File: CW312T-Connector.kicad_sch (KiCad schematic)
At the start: 3 parts, among them P1 PCIEx4 EDGE CONNECTOR

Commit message: updated design - still needs vcc routing
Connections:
- net CLKIN renamed CLKO_FROM_FPGA
- net CLKOUT renamed CLKI_TO_FPGA
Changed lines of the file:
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@@
 		)
 	)
-	(hierarchical_label "CLKIN"
+	(hierarchical_label "CLKO_FROM_FPGA"
 		(shape input)
 		(at 93.98 124.46 180)
@@
 		)
 	)
-	(hierarchical_label "CLKOUT"
+	(hierarchical_label "CLKI_TO_FPGA"
 		(shape input)
 		(at 199.39 119.38 0)

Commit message: updated schematic and pcb, fixed silkscreen - Ready for review
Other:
- moved on the sheet: R12, R13

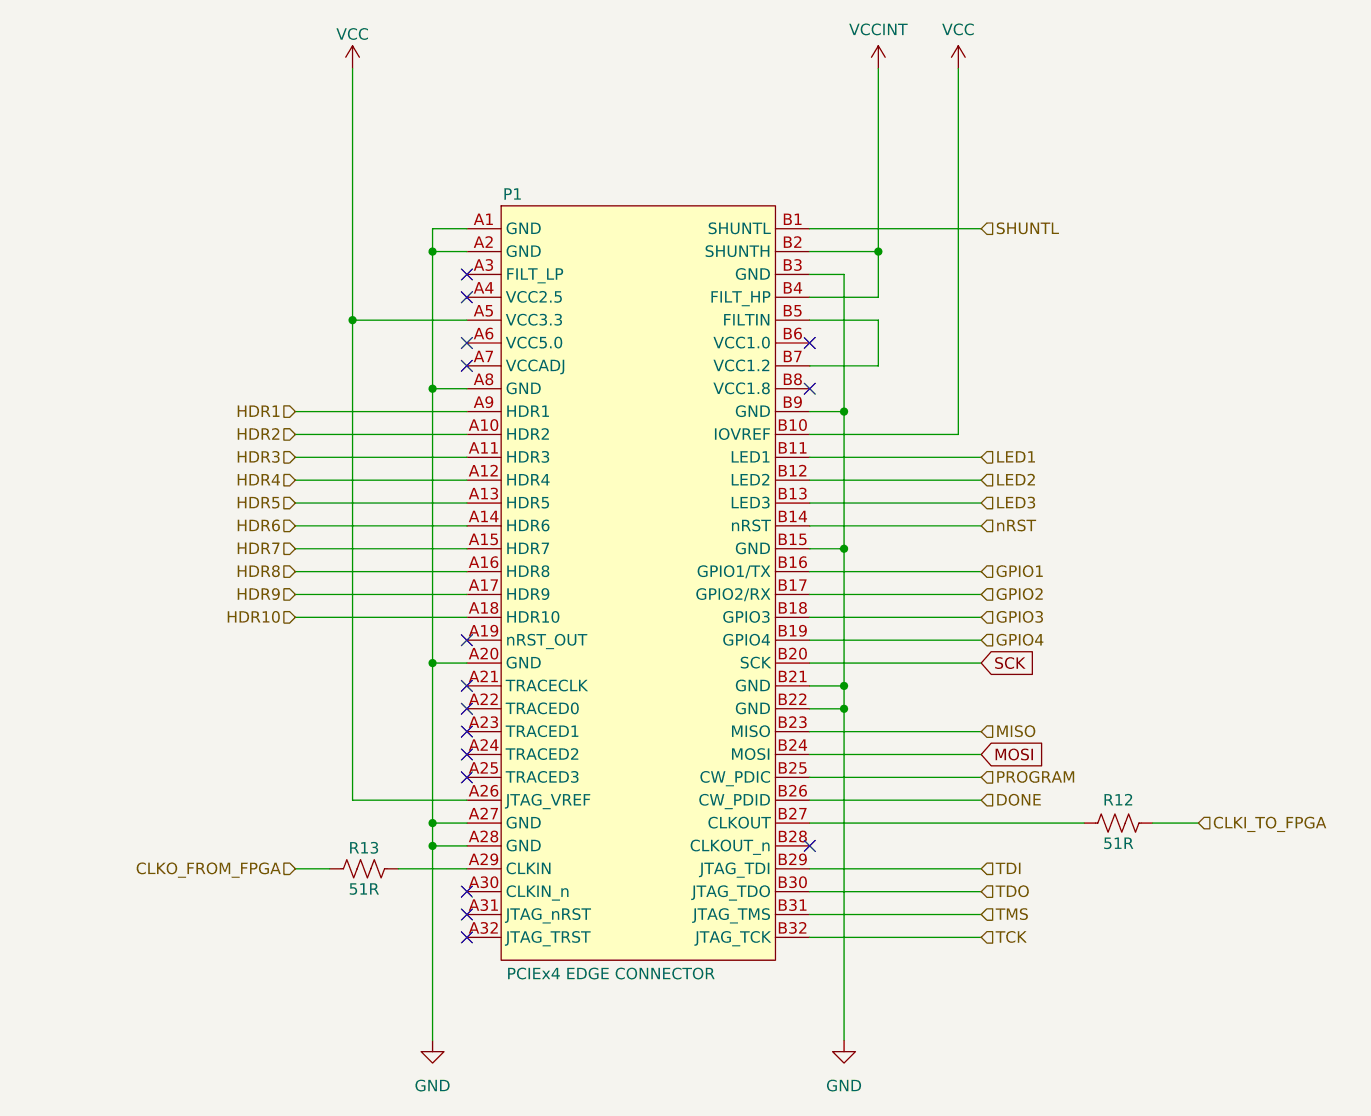
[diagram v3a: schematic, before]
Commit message: updated schematic and pcb after library re-organization
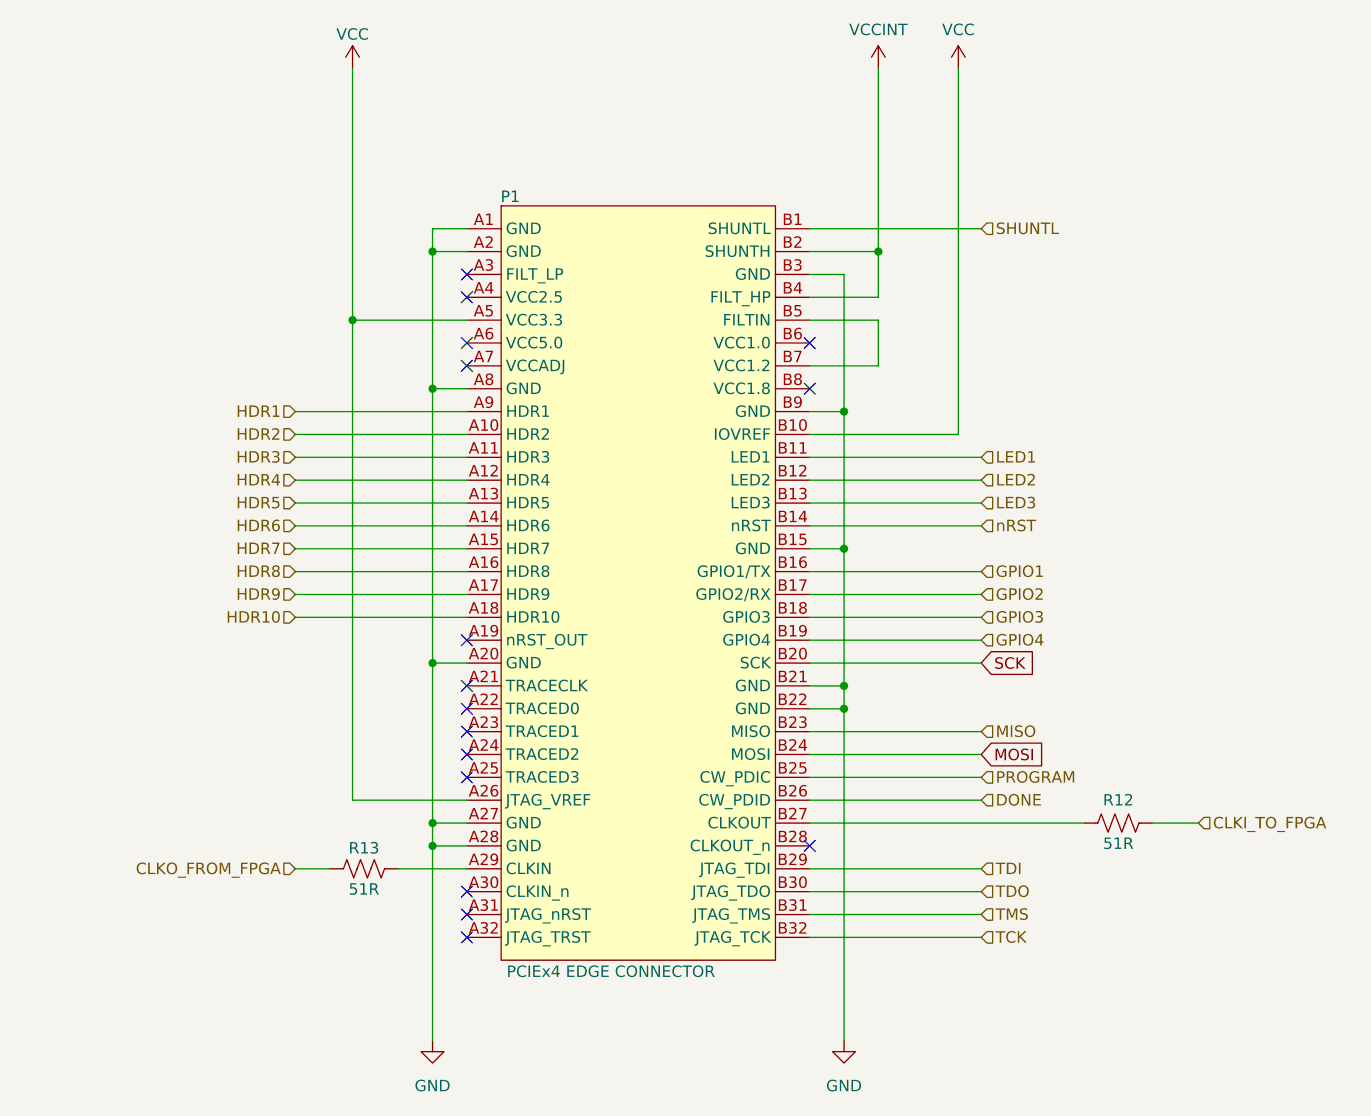
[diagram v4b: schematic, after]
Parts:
- removed P1: PCIEx4 EDGE CONNECTOR, tutorial_2_library:CW312_Template, symbol tutorial_2_library:CW312T-Template
- added P1: PCIEx4 EDGE CONNECTOR, tutorial_2_library:CW312_Template, symbol Connectors:CW312T-Template
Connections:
- net DONE: now also P1.B26 (CW_PDID)
- net GND: now also P1.A1 (GND), P1.A2 (GND), P1.A20 (GND), P1.A27 (GND), P1.A28 (GND), P1.A8 (GND), P1.B15 (GND), P1.B21 (GND), P1.B22 (GND), P1.B3 (GND), P1.B9 (GND)
- net GPIO1: now also P1.B16 (GPIO1/TX)
- net GPIO2: now also P1.B17 (GPIO2/RX)
- net GPIO3: now also P1.B18 (GPIO3)
- net GPIO4: now also P1.B19 (GPIO4)
- net HDR1: now also P1.A9 (HDR1)
- net HDR10: now also P1.A18 (HDR10)
- net HDR2: now also P1.A10 (HDR2)
- net HDR3: now also P1.A11 (HDR3)
- net HDR4: now also P1.A12 (HDR4)
- net HDR5: now also P1.A13 (HDR5)
- net HDR6: now also P1.A14 (HDR6)
- net HDR7: now also P1.A15 (HDR7)
- net HDR8: now also P1.A16 (HDR8)
- net HDR9: now also P1.A17 (HDR9)
- net LED1: now also P1.B11 (LED1)
- net LED2: now also P1.B12 (LED2)
- net LED3: now also P1.B13 (LED3)
- net MISO: now also P1.B23 (MISO)
- net MOSI: now also P1.B24 (MOSI)
- net PROGRAM: now also P1.B25 (CW_PDIC)
- net SCK: now also P1.B20 (SCK)
- net SHUNTL: now also P1.B1 (SHUNTL)
- net TCK: now also P1.B32 (JTAG_TCK)
- net TDI: now also P1.B29 (JTAG_TDI)
- net TDO: now also P1.B30 (JTAG_TDO)
- net TMS: now also P1.B31 (JTAG_TMS)
- net VCC: now also P1.A26 (JTAG_VREF), P1.A5 (VCC3.3), P1.B10 (IOVREF)
- net VCCINT: now also P1.B2 (SHUNTH), P1.B4 (FILT_HP)
- net nRST: now also P1.B14 (nRST)
- net at R13.2: now also P1.A29 (CLKIN)
- net at R12.1: now also P1.B27 (CLKOUT)
- new net: P1.B5 (FILTIN), P1.B7 (VCC1.2)
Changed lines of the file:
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@@
-	)
-	(symbol
-		(lib_id "tutorial_2_library:CW312T-Template")
-		(at 142.24 53.34 0)
-		(unit 1)
-		(exclude_from_sim no)
-		(in_bom no)
-		(on_board yes)
-		(dnp no)
-		(property "Reference" "P1"
-			(at 128.27 49.53 0)
-			(effects
-				(font
-					(size 1.27 1.27)
-				)
-			)
-		)
-		(property "Value" "PCIEx4 EDGE CONNECTOR"
-			(at 139.192 136.144 0)
-			(effects
-				(font
-					(size 1.27 1.27)
-				)
-			)
-		)
-		(property "Footprint" "tutorial_2_library:CW312_Template"
-			(at 138.43 146.05 0)
-			(effects
-				(font
-					(size 1.27 1.27)
-				)
-				(hide yes)
-			)
-		)
-		(property "Datasheet" ""
-			(at 139.7 52.07 0)
-			(effects
-				(font
-					(size 1.27 1.27)
-				)
-				(hide yes)
-			)
-		)
-		(property "Description" "BOARD AND EDGE CONNECTOR TEMPLATE FOR CW312 TARGETS"
-			(at 151.13 142.24 0)
-			(effects
-				(font
-					(size 1.27 1.27)
-				)
-				(hide yes)
-			)
-		)
-		(pin "B27"
-		)
-		(pin "B28"
-		)
-		(pin "B32"
-		)
-		(pin "B6"
-		)
-		(pin "B9"
-		)
-		(pin "B7"
-		)
-		(pin "B30"
-		)
-		(pin "B31"
-		)
-		(pin "B26"
-		)
-		(pin "B4"
-		)
-		(pin "B3"
-		)
-		(pin "B5"
-		)
-		(pin "B8"
-		)
-		(pin "B29"
-		)
-		(pin "B18"
-		)
-		(pin "B19"
-		)
-		(pin "A1"
-		)
-		(pin "A6"
-		)
-		(pin "B15"
-		)
-		(pin "A20"
-		)
-		(pin "A16"
-		)
-		(pin "A9"
-		)
-		(pin "B2"
-		)
-		(pin "B20"
-		)
-		(pin "A24"
-		)
-		(pin "A29"
-		)
-		(pin "B21"
-		)
-		(pin "B13"
-		)
-		(pin "A14"
-		)
-		(pin "A21"
-		)
-		(pin "B22"
-		)
-		(pin "B23"
-		)
-		(pin "A32"
-		)
-		(pin "B24"
-		)
-		(pin "B25"
-		)
-		(pin "A12"
-		)
-		(pin "A18"
-		)
-		(pin "A23"
-		)
-		(pin "A15"
-		)
-		(pin "A26"
-		)
-		(pin "A8"
-		)
-		(pin "A13"
-		)
-		(pin "A2"
-		)
-		(pin "A28"
-		)
-		(pin "A31"
-		)
-		(pin "A7"
-		)
-		(pin "B16"
-		)
-		(pin "A10"
-		)
-		(pin "A3"
-		)
-		(pin "A11"
-		)
-		(pin "A19"
-		)
-		(pin "A17"
-		)
-		(pin "A4"
-		)
-		(pin "A25"
-		)
-		(pin "B10"
-		)
-		(pin "B11"
-		)
-		(pin "B14"
-		)
-		(pin "A30"
-		)
-		(pin "A22"
-		)
-		(pin "B12"
-		)
-		(pin "B1"
-		)
-		(pin "B17"
-		)
-		(pin "A5"
-		)
-		(pin "A27"
-		)
-		(instances
-			(project ""
-				(path "/06b23300-1735-453c-a53d-6066ed551221/6361a6c9-79c6-4b34-90f7-819ffa6ef97b"
-					(reference "P1")
-					(unit 1)
-				)
-			)
-		)
 	)
 	(symbol
@@
 					(unit 1)
 				)
+			)
+		)
+	)
+	(symbol
+		(lib_id "Connectors:CW312T-Template")
+		(at 142.24 53.34 0)
+		(unit 1)
+		(exclude_from_sim no)
+		(in_bom no)
+		(on_board yes)
+		(dnp no)
+		(property "Reference" "P1"
+			(at 128.016 49.784 0)
+			(effects
+				(font
+					(size 1.27 1.27)
+				)
+			)
+		)
+		(property "Value" "PCIEx4 EDGE CONNECTOR"
+			(at 139.192 135.89 0)
+			(effects
+				(font
+					(size 1.27 1.27)
+				)
+			)
+		)
+		(property "Footprint" "tutorial_2_library:CW312_Template"
+			(at 138.43 146.05 0)
+			(effects
+				(font
+					(size 1.27 1.27)
+				)
+				(hide yes)
+			)
+		)
+		(property "Datasheet" ""
+			(at 139.7 52.07 0)
+			(effects
+				(font
+					(size 1.27 1.27)
+				)
+				(hide yes)
+			)
+		)
+		(property "Description" "BOARD AND EDGE CONNECTOR TEMPLATE FOR CW312 TARGETS"
+			(at 151.13 142.24 0)
+			(effects
+				(font
+					(size 1.27 1.27)
+				)
+				(hide yes)
+			)
+		)
+		(pin "B10"
+		)
+		(pin "A17"
+		)
+		(pin "A1"
+		)
+		(pin "A6"
+		)
+		(pin "A3"
+		)
+		(pin "A14"
+		)
+		(pin "A26"
+		)
+		(pin "A11"
+		)
+		(pin "A13"
+		)
+		(pin "A16"
+		)
+		(pin "A18"
+		)
+		(pin "A20"
+		)
+		(pin "A10"
+		)
+		(pin "A29"
+		)
+		(pin "A32"
+		)
+		(pin "A5"
+		)
+		(pin "A7"
+		)
+		(pin "A28"
+		)
+		(pin "A8"
+		)
+		(pin "B1"
+		)
+		(pin "A25"
+		)
+		(pin "A4"
+		)
+		(pin "B11"
+		)
+		(pin "A19"
+		)
+		(pin "A23"
+		)
+		(pin "B2"
+		)
+		(pin "A9"
+		)
+		(pin "A30"
+		)
+		(pin "A24"
+		)
+		(pin "A31"
+		)
+		(pin "A15"
+		)
+		(pin "A12"
+		)
+		(pin "A2"
+		)
+		(pin "A21"
+		)
+		(pin "A22"
+		)
+		(pin "A27"
+		)
+		(pin "B29"
+		)
+		(pin "B20"
+		)
+		(pin "B8"
+		)
+		(pin "B24"
+		)
+		(pin "B4"
+		)
+		(pin "B7"
+		)
+		(pin "B13"
+		)
+		(pin "B17"
+		)
+		(pin "B3"
+		)
+		(pin "B26"
+		)
+		(pin "B31"
+		)
+		(pin "B16"
+		)
+		(pin "B12"
+		)
+		(pin "B5"
+		)
+		(pin "B30"
+		)
+		(pin "B19"
+		)
+		(pin "B32"
+		)
+		(pin "B9"
+		)
+		(pin "B21"
+		)
+		(pin "B28"
+		)
+		(pin "B15"
+		)
+		(pin "B6"
+		)
+		(pin "B18"
+		)
+		(pin "B23"
+		)
+		(pin "B14"
+		)
+		(pin "B22"
+		)
+		(pin "B27"
+		)
+		(pin "B25"
+		)
+		(instances
+			(project ""
+				(path "/06b23300-1735-453c-a53d-6066ed551221/6361a6c9-79c6-4b34-90f7-819ffa6ef97b"
+					(reference "P1")
+					(unit 1)
+				)
